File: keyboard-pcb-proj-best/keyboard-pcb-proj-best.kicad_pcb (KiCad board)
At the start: 2 copper layers, 24 parts, among them SW1 SW_PUSH, U1 ATmega32U4-A, Y1 16Mhz

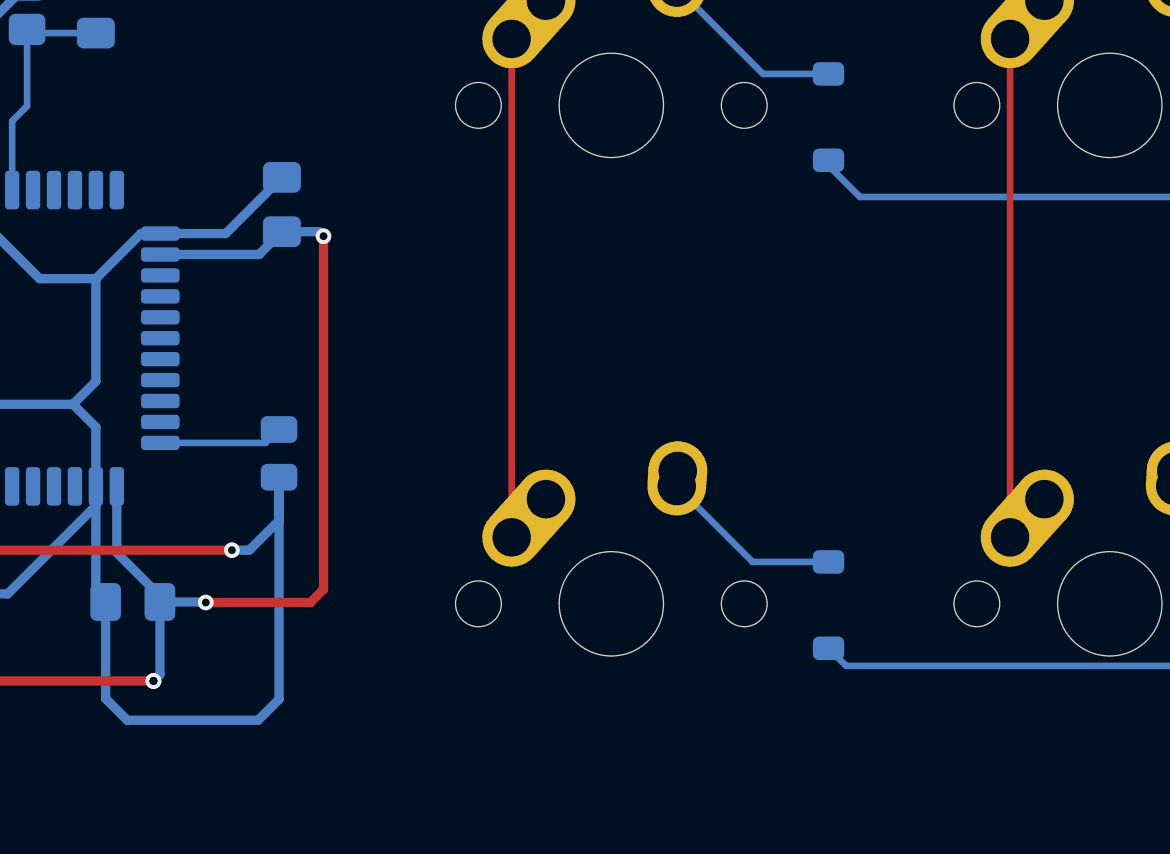
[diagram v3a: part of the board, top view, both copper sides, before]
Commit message: Finalized Routing and Matrix Pin Out
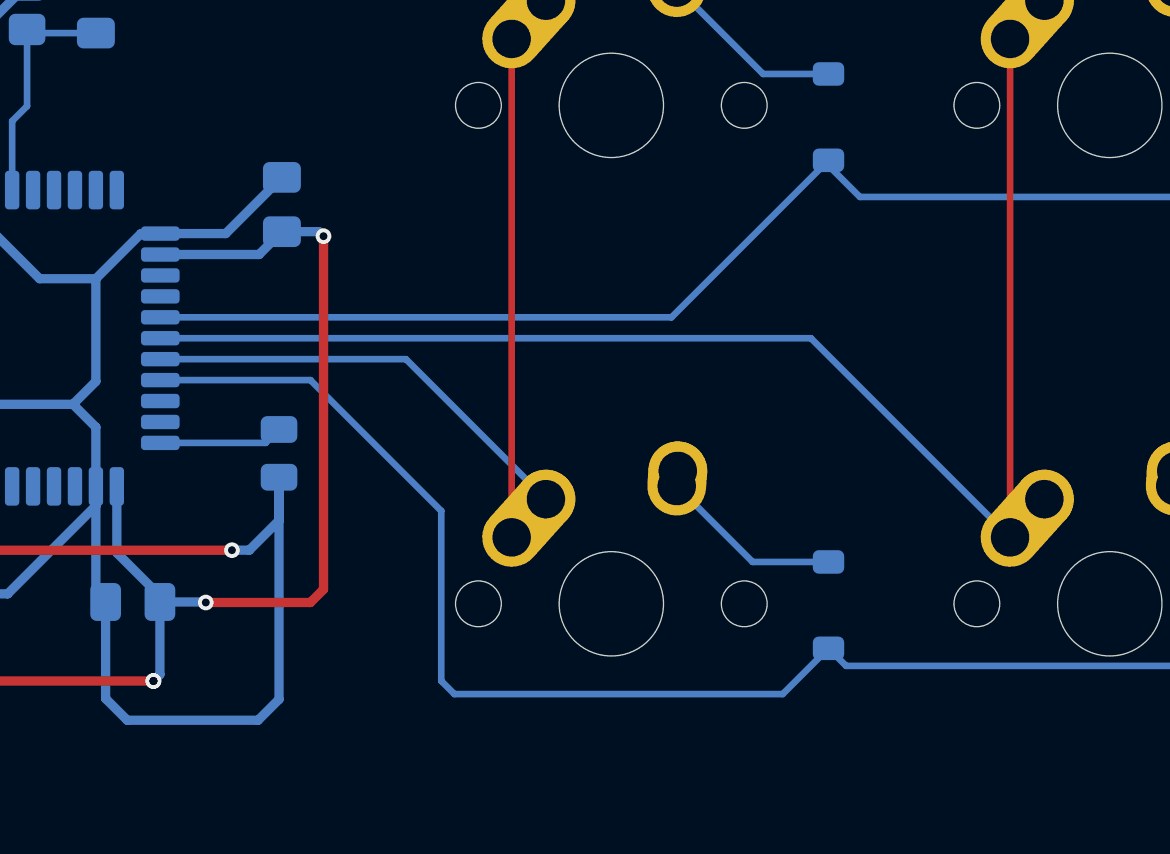
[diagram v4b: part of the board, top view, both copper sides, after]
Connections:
- U1 pad 27: unconnected-(U1-PD7-Pad27) -> ROW0
- U1 pad 28: unconnected-(U1-PB4-Pad28) -> COL1
- U1 pad 29: unconnected-(U1-PB5-Pad29) -> COL0
- U1 pad 30: unconnected-(U1-PB6-Pad30) -> ROW1
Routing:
- net COL1: track 19.1 -> 54.7 mm
- net ROW1: track 19.7 -> 54.7 mm
- net ROW0: track 20.4 -> 48.4 mm
- net COL0: track 19.1 -> 36.0 mm
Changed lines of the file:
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@@
 	(net 21 "unconnected-(U1-PF4-Pad39)")
 	(net 22 "unconnected-(U1-PF5-Pad38)")
-	(net 23 "unconnected-(U1-PB6-Pad30)")
-	(net 24 "unconnected-(U1-PF6-Pad37)")
-	(net 25 "unconnected-(U1-PC6-Pad31)")
-	(net 26 "unconnected-(U1-AREF-Pad42)")
-	(net 27 "unconnected-(U1-PF0-Pad41)")
-	(net 28 "unconnected-(U1-PB4-Pad28)")
-	(net 29 "unconnected-(U1-PB1-Pad9)")
-	(net 30 "unconnected-(U1-PD5-Pad22)")
-	(net 31 "unconnected-(U1-PB3-Pad11)")
-	(net 32 "unconnected-(U1-PF1-Pad40)")
-	(net 33 "unconnected-(U1-PD2-Pad20)")
-	(net 34 "unconnected-(U1-PE6-Pad1)")
-	(net 35 "unconnected-(U1-PD6-Pad26)")
-	(net 36 "unconnected-(U1-PB5-Pad29)")
-	(net 37 "unconnected-(U1-PB0-Pad8)")
-	(net 38 "unconnected-(U1-PF7-Pad36)")
-	(net 39 "unconnected-(U1-PB2-Pad10)")
-	(net 40 "unconnected-(U1-PC7-Pad32)")
-	(net 41 "unconnected-(U1-PD4-Pad25)")
-	(net 42 "unconnected-(U1-PB7-Pad12)")
-	(net 43 "unconnected-(U1-PD7-Pad27)")
-	(net 44 "unconnected-(U1-PD0-Pad18)")
-	(net 45 "unconnected-(U1-PD1-Pad19)")
-	(net 46 "unconnected-(U1-PD3-Pad21)")
-	(net 47 "unconnected-(USB1-SHIELD-Pad6)")
-	(net 48 "unconnected-(USB1-ID-Pad2)")
+	(net 23 "unconnected-(U1-PF6-Pad37)")
+	(net 24 "unconnected-(U1-PC6-Pad31)")
+	(net 25 "unconnected-(U1-AREF-Pad42)")
+	(net 26 "unconnected-(U1-PF0-Pad41)")
+	(net 27 "unconnected-(U1-PB1-Pad9)")
+	(net 28 "unconnected-(U1-PD5-Pad22)")
+	(net 29 "unconnected-(U1-PB3-Pad11)")
+	(net 30 "unconnected-(U1-PF1-Pad40)")
+	(net 31 "unconnected-(U1-PD2-Pad20)")
+	(net 32 "unconnected-(U1-PE6-Pad1)")
+	(net 33 "unconnected-(U1-PD6-Pad26)")
+	(net 34 "unconnected-(U1-PB0-Pad8)")
+	(net 35 "unconnected-(U1-PF7-Pad36)")
+	(net 36 "unconnected-(U1-PB2-Pad10)")
+	(net 37 "unconnected-(U1-PC7-Pad32)")
+	(net 38 "unconnected-(U1-PD4-Pad25)")
+	(net 39 "unconnected-(U1-PB7-Pad12)")
+	(net 40 "unconnected-(U1-PD0-Pad18)")
+	(net 41 "unconnected-(U1-PD1-Pad19)")
+	(net 42 "unconnected-(U1-PD3-Pad21)")
+	(net 43 "unconnected-(USB1-SHIELD-Pad6)")
+	(net 44 "unconnected-(USB1-ID-Pad2)")
 	(footprint "MX_Alps_Hybrid:MX-1U-NoLED"
 		(layer "F.Cu")
@@
 			(layers "B.Cu" "B.Mask" "B.Paste")
 			(roundrect_rratio 0.25)
-			(net 34 "unconnected-(U1-PE6-Pad1)")
+			(net 32 "unconnected-(U1-PE6-Pad1)")
 			(pinfunction "PE6")
 			(pintype "bidirectional")
@@
 			(layers "B.Cu" "B.Mask" "B.Paste")
 			(roundrect_rratio 0.25)
-			(net 37 "unconnected-(U1-PB0-Pad8)")
+			(net 34 "unconnected-(U1-PB0-Pad8)")
 			(pinfunction "PB0")
 			(pintype "bidirectional")
@@
 			(layers "B.Cu" "B.Mask" "B.Paste")
 			(roundrect_rratio 0.25)
-			(net 29 "unconnected-(U1-PB1-Pad9)")
+			(net 27 "unconnected-(U1-PB1-Pad9)")
 			(pinfunction "PB1")
 			(pintype "bidirectional")
@@
 			(layers "B.Cu" "B.Mask" "B.Paste")
 			(roundrect_rratio 0.25)
-			(net 39 "unconnected-(U1-PB2-Pad10)")
+			(net 36 "unconnected-(U1-PB2-Pad10)")
 			(pinfunction "PB2")
 			(pintype "bidirectional")
@@
 			(layers "B.Cu" "B.Mask" "B.Paste")
 			(roundrect_rratio 0.25)
-			(net 31 "unconnected-(U1-PB3-Pad11)")
+			(net 29 "unconnected-(U1-PB3-Pad11)")
 			(pinfunction "PB3")
 			(pintype "bidirectional")
@@
 			(layers "B.Cu" "B.Mask" "B.Paste")
 			(roundrect_rratio 0.25)
-			(net 42 "unconnected-(U1-PB7-Pad12)")
+			(net 39 "unconnected-(U1-PB7-Pad12)")
 			(pinfunction "PB7")
 			(pintype "bidirectional")
@@
 			(layers "B.Cu" "B.Mask" "B.Paste")
 			(roundrect_rratio 0.25)
-			(net 44 "unconnected-(U1-PD0-Pad18)")
+			(net 40 "unconnected-(U1-PD0-Pad18)")
 			(pinfunction "PD0")
 			(pintype "bidirectional")
@@
 			(layers "B.Cu" "B.Mask" "B.Paste")
 			(roundrect_rratio 0.25)
-			(net 45 "unconnected-(U1-PD1-Pad19)")
+			(net 41 "unconnected-(U1-PD1-Pad19)")
 			(pinfunction "PD1")
 			(pintype "bidirectional")
@@
 			(layers "B.Cu" "B.Mask" "B.Paste")
 			(roundrect_rratio 0.25)
-			(net 33 "unconnected-(U1-PD2-Pad20)")
+			(net 31 "unconnected-(U1-PD2-Pad20)")
 			(pinfunction "PD2")
 			(pintype "bidirectional")
@@
 			(layers "B.Cu" "B.Mask" "B.Paste")
 			(roundrect_rratio 0.25)
-			(net 46 "unconnected-(U1-PD3-Pad21)")
+			(net 42 "unconnected-(U1-PD3-Pad21)")
 			(pinfunction "PD3")
 			(pintype "bidirectional")
@@
 			(layers "B.Cu" "B.Mask" "B.Paste")
 			(roundrect_rratio 0.25)
-			(net 30 "unconnected-(U1-PD5-Pad22)")
+			(net 28 "unconnected-(U1-PD5-Pad22)")
 			(pinfunction "PD5")
 			(pintype "bidirectional")
@@
 			(layers "B.Cu" "B.Mask" "B.Paste")
 			(roundrect_rratio 0.25)
-			(net 41 "unconnected-(U1-PD4-Pad25)")
+			(net 38 "unconnected-(U1-PD4-Pad25)")
 			(pinfunction "PD4")
 			(pintype "bidirectional")
@@
 			(layers "B.Cu" "B.Mask" "B.Paste")
 			(roundrect_rratio 0.25)
-			(net 35 "unconnected-(U1-PD6-Pad26)")
+			(net 33 "unconnected-(U1-PD6-Pad26)")
 			(pinfunction "PD6")
 			(pintype "bidirectional")
@@
 			(layers "B.Cu" "B.Mask" "B.Paste")
 			(roundrect_rratio 0.25)
-			(net 43 "unconnected-(U1-PD7-Pad27)")
+			(net 7 "ROW0")
 			(pinfunction "PD7")
 			(pintype "bidirectional")
@@
 			(layers "B.Cu" "B.Mask" "B.Paste")
 			(roundrect_rratio 0.25)
-			(net 28 "unconnected-(U1-PB4-Pad28)")
+			(net 14 "COL1")
 			(pinfunction "PB4")
 			(pintype "bidirectional")
@@
 			(layers "B.Cu" "B.Mask" "B.Paste")
 			(roundrect_rratio 0.25)
-			(net 36 "unconnected-(U1-PB5-Pad29)")
+			(net 13 "COL0")
 			(pinfunction "PB5")
 			(pintype "bidirectional")
@@
 			(layers "B.Cu" "B.Mask" "B.Paste")
 			(roundrect_rratio 0.25)
-			(net 23 "unconnected-(U1-PB6-Pad30)")
+			(net 9 "ROW1")
 			(pinfunction "PB6")
 			(pintype "bidirectional")
@@
 			(layers "B.Cu" "B.Mask" "B.Paste")
 			(roundrect_rratio 0.25)
-			(net 25 "unconnected-(U1-PC6-Pad31)")
+			(net 24 "unconnected-(U1-PC6-Pad31)")
 			(pinfunction "PC6")
 			(pintype "bidirectional")
@@
 			(layers "B.Cu" "B.Mask" "B.Paste")
 			(roundrect_rratio 0.25)
-			(net 40 "unconnected-(U1-PC7-Pad32)")
+			(net 37 "unconnected-(U1-PC7-Pad32)")
 			(pinfunction "PC7")
 			(pintype "bidirectional")
@@
 			(layers "B.Cu" "B.Mask" "B.Paste")
 			(roundrect_rratio 0.25)
-			(net 38 "unconnected-(U1-PF7-Pad36)")
+			(net 35 "unconnected-(U1-PF7-Pad36)")
 			(pinfunction "PF7")
 			(pintype "bidirectional")
@@
 			(layers "B.Cu" "B.Mask" "B.Paste")
 			(roundrect_rratio 0.25)
-			(net 24 "unconnected-(U1-PF6-Pad37)")
+			(net 23 "unconnected-(U1-PF6-Pad37)")
 			(pinfunction "PF6")
 			(pintype "bidirectional")
@@
 			(layers "B.Cu" "B.Mask" "B.Paste")
 			(roundrect_rratio 0.25)
-			(net 32 "unconnected-(U1-PF1-Pad40)")
+			(net 30 "unconnected-(U1-PF1-Pad40)")
 			(pinfunction "PF1")
 			(pintype "bidirectional")
@@
 			(layers "B.Cu" "B.Mask" "B.Paste")
 			(roundrect_rratio 0.25)
-			(net 27 "unconnected-(U1-PF0-Pad41)")
+			(net 26 "unconnected-(U1-PF0-Pad41)")
 			(pinfunction "PF0")
 			(pintype "bidirectional")
@@
 			(layers "B.Cu" "B.Mask" "B.Paste")
 			(roundrect_rratio 0.25)
-			(net 26 "unconnected-(U1-AREF-Pad42)")
+			(net 25 "unconnected-(U1-AREF-Pad42)")
 			(pinfunction "AREF")
 			(pintype "passive")
@@
 			(size 2.25 0.5)
 			(layers "B.Cu" "B.Mask" "B.Paste")
-			(net 48 "unconnected-(USB1-ID-Pad2)")
+			(net 44 "unconnected-(USB1-ID-Pad2)")
 			(pinfunction "ID")
 			(pintype "input")
@@
 			(layers "*.Cu" "*.Mask")
 			(remove_unused_layers no)
-			(net 47 "unconnected-(USB1-SHIELD-Pad6)")
+			(net 43 "unconnected-(USB1-SHIELD-Pad6)")
 			(pinfunction "SHIELD")
 			(pintype "input")
@@
 			(layers "*.Cu" "*.Mask")
 			(remove_unused_layers no)
-			(net 47 "unconnected-(USB1-SHIELD-Pad6)")
+			(net 43 "unconnected-(USB1-SHIELD-Pad6)")
 			(pinfunction "SHIELD")
 			(pintype "input")
@@
 			(layers "*.Cu" "*.Mask")
 			(remove_unused_layers no)
-			(net 47 "unconnected-(USB1-SHIELD-Pad6)")
+			(net 43 "unconnected-(USB1-SHIELD-Pad6)")
 			(pinfunction "SHIELD")
 			(pintype "input")
@@
 			(layers "*.Cu" "*.Mask")
 			(remove_unused_layers no)
-			(net 47 "unconnected-(USB1-SHIELD-Pad6)")
+			(net 43 "unconnected-(USB1-SHIELD-Pad6)")
 			(pinfunction "SHIELD")
 			(pintype "input")
@@
 	)
 	(segment
+		(start 108.2625 99.6)
+		(end 127.8 99.6)
+		(width 0.254)
+		(layer "B.Cu")
+		(net 7)
+	)
+	(segment
+		(start 127.8 99.6)
+		(end 133.8 93.6)
+		(width 0.254)
+		(layer "B.Cu")
+		(net 7)
+	)
+	(segment
 		(start 151.5 95)
 		(end 152.78 93.72)
@@
 	)
 	(segment
+		(start 108.2625 102)
+		(end 114 102)
+		(width 0.254)
+		(layer "B.Cu")
+		(net 9)
+	)
+	(segment
 		(start 133.8 112.25)
 		(end 134.4719 112.9219)
@@
 	)
 	(segment
+		(start 114 102)
+		(end 119 107)
+		(width 0.254)
+		(layer "B.Cu")
+		(net 9)
+	)
+	(segment
+		(start 119 113.5)
+		(end 119.5 114)
+		(width 0.254)
+		(layer "B.Cu")
+		(net 9)
+	)
+	(segment
 		(start 134.4719 112.9219)
 		(end 152.1256 112.9219)
@@
 	)
 	(segment
+		(start 119.5 114)
+		(end 132.05 114)
+		(width 0.254)
+		(layer "B.Cu")
+		(net 9)
+	)
+	(segment
+		(start 119 107)
+		(end 119 113.5)
+		(width 0.254)
+		(layer "B.Cu")
+		(net 9)
+	)
+	(segment
 		(start 152.1256 112.9219)
 		(end 152.89 112.1575)
@@
 	)
 	(segment
+		(start 132.05 114)
+		(end 133.8 112.25)
+		(width 0.254)
+		(layer "B.Cu")
+		(net 9)
+	)
+	(segment
 		(start 130.9 108.95)
 		(end 128 106.05)
@@
 	)
 	(segment
+		(start 108.2625 101.2)
+		(end 117.65 101.2)
+		(width 0.254)
+		(layer "B.Cu")
+		(net 13)
+	)
+	(segment
+		(start 117.65 101.2)
+		(end 123 106.55)
+		(width 0.254)
+		(layer "B.Cu")
+		(net 13)
+	)
+	(segment
 		(start 140.74 88.96)
 		(end 140.74 108.01)
@@
 		(net 14)
 	)
+	(segment
+		(start 133.13 100.4)
+		(end 140.74 108.01)
+		(width 0.254)
+		(layer "B.Cu")
+		(net 14)
+	)
+	(segment
+		(start 108.2625 100.4)
+		(end 133.13 100.4)
+		(width 0.254)
+		(layer "B.Cu")
+		(net 14)
+	)

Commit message: Completed Board Design
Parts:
- moved D4 0.89 mm to (152.0, 110.5)
- moved D2 0.78 mm to (152.0, 91.8)
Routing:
- net GND: track 205.1 -> 198.7 mm
- net ROW1: track 54.7 -> 53.8 mm
- net Net-(D2-A): track 7.07 -> 6.28 mm
- added copper zone on B.Cu, net GND
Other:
- board outline added: 86 x 38.5 mm
- board text added: "T-T Board"
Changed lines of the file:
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@@
 	(footprint "Diode_SMD:D_SOD-123"
 		(layer "B.Cu")
-		(at 152.78 91.8875 90)
+		(at 152 91.85 90)
 		(descr "SOD-123")
 		(tags "SOD-123")
@@
 	(footprint "Diode_SMD:D_SOD-123"
 		(layer "B.Cu")
-		(at 152.89 110.5075 90)
+		(at 152 110.5075 90)
 		(descr "SOD-123")
 		(tags "SOD-123")
@@
 	)
 	(gr_line
-		(start 81.9 120.5)
-		(end 70.1 120.5)
+		(start 82 82)
+		(end 152 82)
 		(stroke
 			(width 0.2)
@@
 	)
 	(gr_line
-		(start 82 82)
-		(end 152 82)
+		(start 152 120.5)
+		(end 82 120.5)
 		(stroke
 			(width 0.2)
@@
 	)
 	(gr_line
-		(start 154 84)
-		(end 154 118.5)
+		(start 82 82)
+		(end 70.2 82)
 		(stroke
 			(width 0.2)
@@
 		(layer "F.Cu")
 	)
-	(gr_line
-		(start 152 120.5)
-		(end 82 120.5)
+	(gr_arc
+		(start 154 118.5)
+		(mid 153.414214 119.914214)
+		(end 152 120.5)
 		(stroke
 			(width 0.2)
@@
 		(layer "F.Cu")
 	)
+	(gr_line
+		(start 70 82)
+		(end 152 82)
+		(stroke
+			(width 0.05)
+			(type default)
+		)
+		(layer "Edge.Cuts")
+	)
 	(gr_arc
-		(start 152 82)
-		(mid 153.414214 82.585786)
-		(end 154 84)
+		(start 154 118.5)
+		(mid 153.414214 119.914214)
+		(end 152 120.5)
 		(stroke
-			(width 0.2)
+			(width 0.05)
 			(type default)
 		)
-		(layer "F.Cu")
+		(layer "Edge.Cuts")
+	)
+	(gr_arc
+		(start 70 120.5)
+		(mid 68.585786 119.914214)
+		(end 68 118.5)
+		(stroke
+			(width 0.05)
+			(type default)
+		)
+		(layer "Edge.Cuts")
 	)
 	(gr_line
-		(start 82 82)
-		(end 70.2 82)
+		(start 154 84)
+		(end 154 118.5)
 		(stroke
-			(width 0.2)
+			(width 0.05)
 			(type default)
 		)
-		(layer "F.Cu")
+		(layer "Edge.Cuts")
 	)
-	(gr_arc
-		(start 68.2 84)
-		(mid 68.785786 82.585786)
-		(end 70.2 82)
+	(gr_line
+		(start 152 120.5)
+		(end 70 120.5)
 		(stroke
-			(width 0.2)
+			(width 0.05)
 			(type default)
 		)
-		(layer "F.Cu")
+		(layer "Edge.Cuts")
 	)
 	(gr_arc
-		(start 70.2 120.5)
-		(mid 68.785786 119.914214)
-		(end 68.2 118.5)
+		(start 152 82)
+		(mid 153.414214 82.585786)
+		(end 154 84)
 		(stroke
-			(width 0.2)
+			(width 0.05)
 			(type default)
 		)
-		(layer "F.Cu")
+		(layer "Edge.Cuts")
 	)
 	(gr_arc
-		(start 154 118.5)
-		(mid 153.414214 119.914214)
-		(end 152 120.5)
+		(start 68 84)
+		(mid 68.585786 82.585786)
+		(end 70 82)
 		(stroke
-			(width 0.2)
+			(width 0.05)
 			(type default)
 		)
-		(layer "F.Cu")
+		(layer "Edge.Cuts")
 	)
 	(gr_line
-		(start 68.2 84)
-		(end 68.2 118.5)
+		(start 68 118.5)
+		(end 68 84)
 		(stroke
-			(width 0.2)
+			(width 0.05)
 			(type default)
 		)
-		(layer "F.Cu")
+		(layer "Edge.Cuts")
+	)
+	(gr_text "T-T Board"
+		(at 105 119 0)
+		(layer "F.SilkS")
+		(effects
+			(font
+				(size 1 1)
+				(thickness 0.1)
+			)
+			(justify left bottom)
+		)
 	)
 	(segment
@@
 	)
 	(segment
-		(start 92 89.925)
-		(end 98.325 89.925)
-		(width 0.3556)
-		(layer "B.Cu")
-		(net 2)
-	)
-	(segment
 		(start 98.4 88.6375)
 		(end 98.4 90)
@@
 	)
 	(segment
+		(start 152 94.5)
+		(end 151.5 95)
+		(width 0.254)
+		(layer "B.Cu")
+		(net 7)
+	)
+	(segment
+		(start 152 93.5)
+		(end 152 94.5)
+		(width 0.254)
+		(layer "B.Cu")
+		(net 7)
+	)
+	(segment
 		(start 133.8 93.6)
 		(end 133.8 93.8)
@@
 	)
 	(segment
-		(start 151.5 95)
-		(end 152.78 93.72)
-		(width 0.254)
-		(layer "B.Cu")
-		(net 7)
-	)
-	(segment
 		(start 133.8 93.8)
 		(end 135 95)
@@
 	)
 	(segment
-		(start 150.2875 90.2375)
-		(end 147.05 87)
+		(start 147.05 87)
+		(end 150.25 90.2)
 		(width 0.254)
 		(layer "B.Cu")
@@
 	)
 	(segment
-		(start 152.78 90.2375)
-		(end 150.2875 90.2375)
+		(start 150.25 90.2)
+		(end 152 90.2)
 		(width 0.254)
 		(layer "B.Cu")
@@
 	)
 	(segment
-		(start 133.8 112.25)
-		(end 134.4719 112.9219)
+		(start 114 102)
+		(end 119 107)
 		(width 0.254)
 		(layer "B.Cu")
@@
 	)
 	(segment
-		(start 114 102)
-		(end 119 107)
+		(start 119 113.5)
+		(end 119.5 114)
 		(width 0.254)
 		(layer "B.Cu")
@@
 	)
 	(segment
-		(start 119 113.5)
-		(end 119.5 114)
+		(start 119.5 114)
+		(end 132.05 114)
 		(width 0.254)
 		(layer "B.Cu")
@@
 	)
 	(segment
-		(start 134.4719 112.9219)
-		(end 152.1256 112.9219)
+		(start 119 107)
+		(end 119 113.5)
 		(width 0.254)
 		(layer "B.Cu")
@@
 	)
 	(segment
-		(start 119.5 114)
-		(end 132.05 114)
+		(start 151.2356 112.9219)
+		(end 134.4719 112.9219)
 		(width 0.254)
 		(layer "B.Cu")
@@
 	)
 	(segment
-		(start 119 107)
-		(end 119 113.5)
+		(start 132.05 114)
+		(end 133.8 112.25)
 		(width 0.254)
 		(layer "B.Cu")
@@
 	)
 	(segment
-		(start 152.1256 112.9219)
-		(end 152.89 112.1575)
+		(start 152 112.1575)
+		(end 151.2356 112.9219)
 		(width 0.254)
 		(layer "B.Cu")
@@
 	)
 	(segment
-		(start 132.05 114)
+		(start 134.4719 112.9219)
 		(end 133.8 112.25)
 		(width 0.254)
@@
 	)
 	(segment
-		(start 149.8575 108.8575)
-		(end 147.05 106.05)
+		(start 147.05 106.05)
+		(end 149.8575 108.8575)
 		(width 0.254)
 		(layer "B.Cu")
@@
 	)
 	(segment
-		(start 152.89 108.8575)
-		(end 149.8575 108.8575)
+		(start 147.05 106.05)
+		(end 147.05 105.51)
+		(width 0.254)
+		(layer "B.Cu")
+		(net 11)
+	)
+	(segment
+		(start 147.05 105.51)
+		(end 147.09 105.47)
+		(width 0.254)
+		(layer "B.Cu")
+		(net 11)
+	)
+	(segment
+		(start 149.8575 108.8575)
+		(end 152 108.8575)
 		(width 0.254)
 		(layer "B.Cu")
@@
 		(net 20)
 	)
+	(zone
+		(net 2)
+		(net_name "GND")
+		(locked yes)
+		(layer "B.Cu")
+		(hatch edge 0.5)
+		(connect_pads
+			(clearance 0.5)
+		)
+		(min_thickness 0.25)
+		(filled_areas_thickness no)
+		(fill yes
+			(thermal_gap 0.5)
+			(thermal_bridge_width 0.5)
+			(smoothing fillet)
+		)
+		(polygon
+			(pts
+				(xy 68 82) (xy 68 120.5) (xy 116 120.5) (xy 116 82)
+			)
+		)
+	)
 	(embedded_fonts no)
